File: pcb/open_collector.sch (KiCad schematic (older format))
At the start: 0 parts

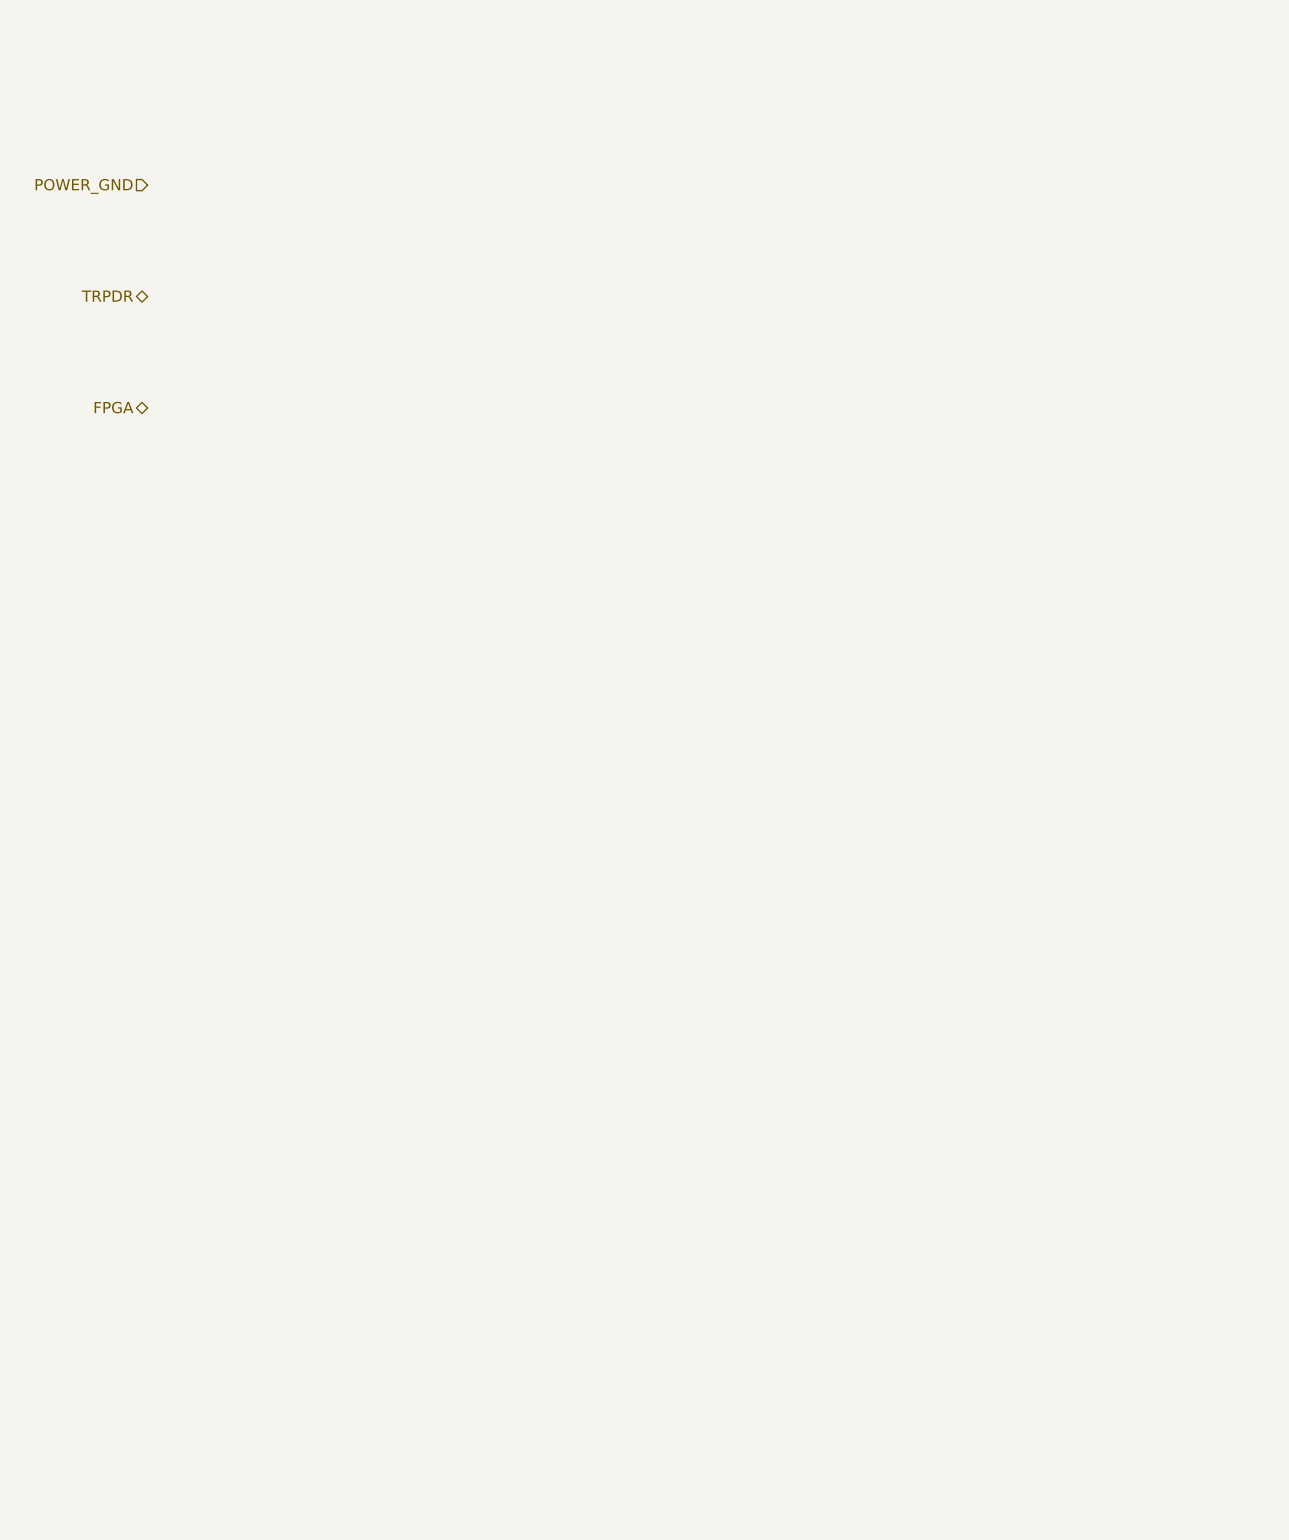
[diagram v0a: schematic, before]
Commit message: some work done on "open collector" list
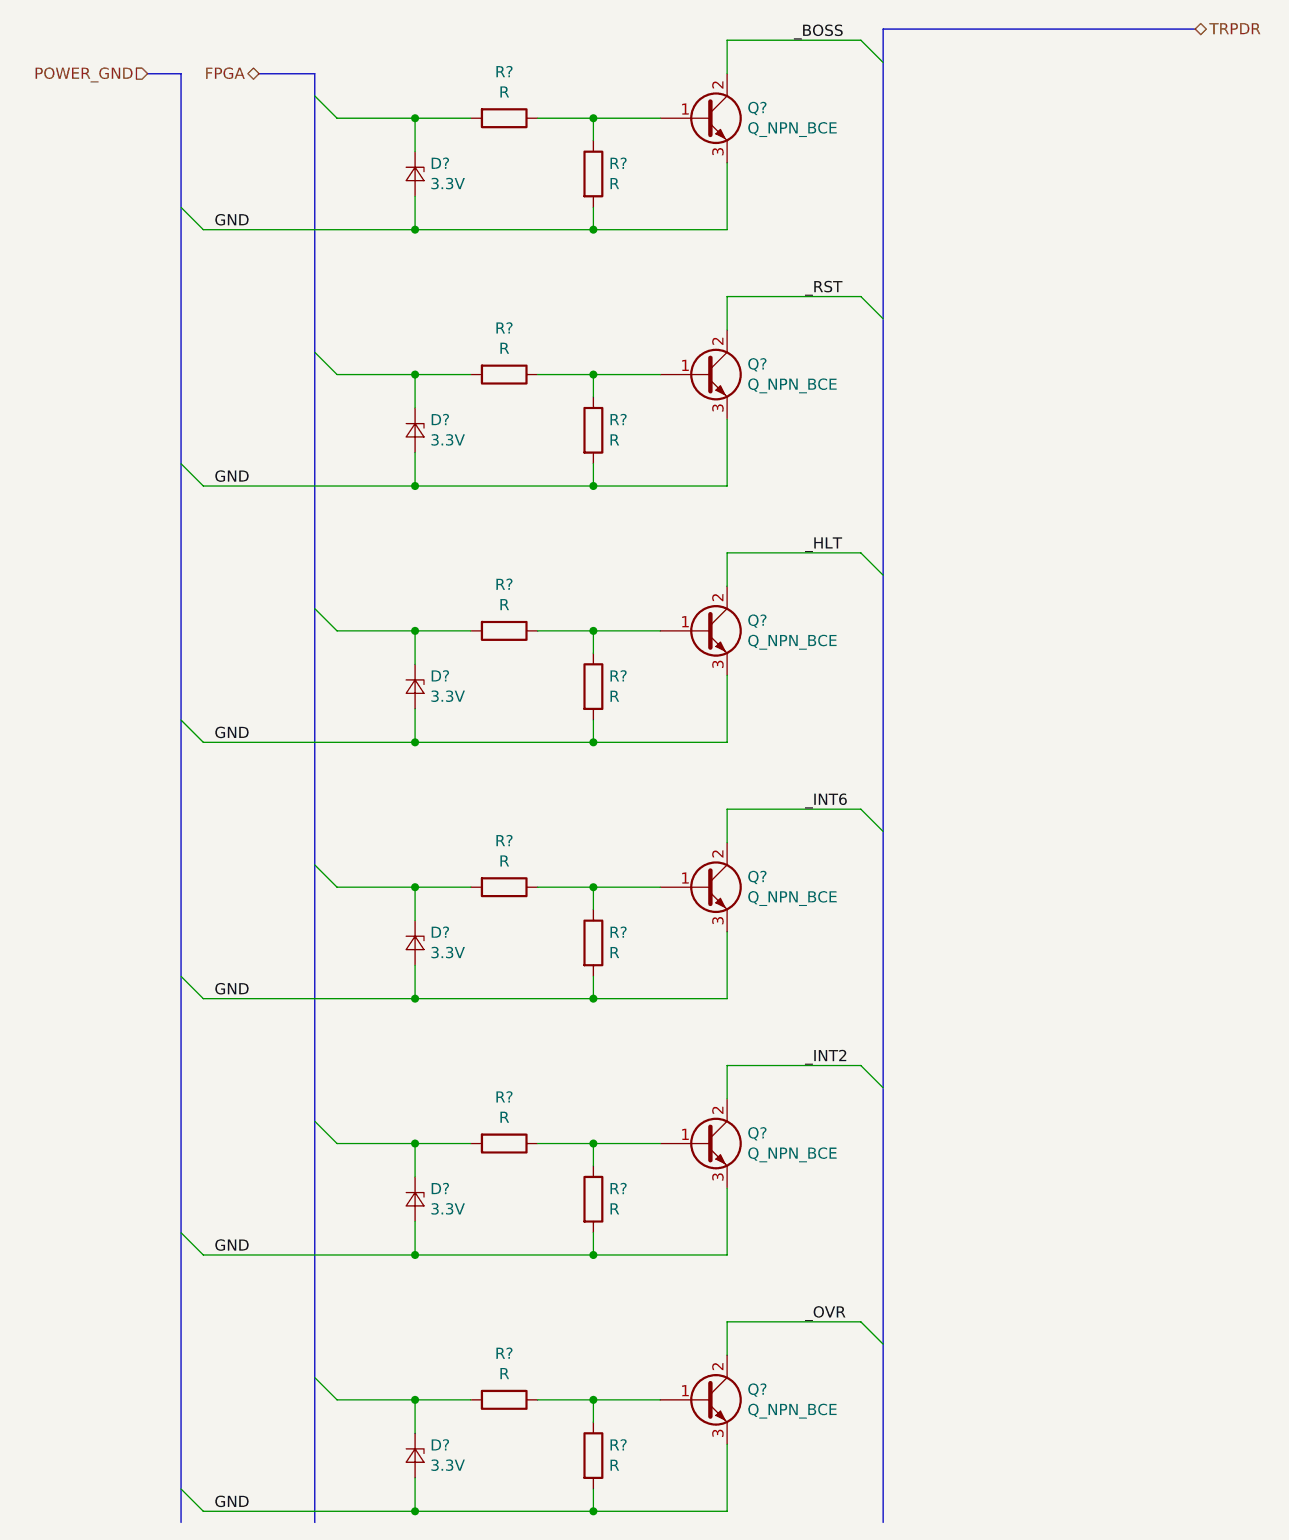
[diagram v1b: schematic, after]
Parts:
- added D? (x6): 3.3V, symbol Device:D_Zener_Small
- added Q? (x6): Q_NPN_BCE, symbol Device:Q_NPN_BCE
- added R? (x12): R, symbol Device:R
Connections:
- new net: Q?.1 (B), R?.1, R?.1 (x6)
- new net: D?.1 (K), R?.2 (x6)
- new net GND: D?.2 (A), D?.2 (A), D?.2 (A), D?.2 (A), D?.2 (A), D?.2 (A), Q?.3 (E), Q?.3 (E), Q?.3 (E), Q?.3 (E), Q?.3 (E), Q?.3 (E), R?.2, R?.2, R?.2, R?.2, R?.2, R?.2
- new net _BOSS: Q?.2 (C)
- new net _HLT: Q?.2 (C)
- new net _INT2: Q?.2 (C)
- new net _INT6: Q?.2 (C)
- new net _OVR: Q?.2 (C)
- new net _RST: Q?.2 (C)
